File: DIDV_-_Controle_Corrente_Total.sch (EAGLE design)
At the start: 135 parts, among them IC401 PIC18F4550_TQFP44, K401 G5L, Q402 BC817, Q501 FZT493, Q502 FZT493, U201 ACS712LC, U202 ACS712LC, U203 ACS712LC, U301 LM35CAZ, U302 LM35CAZ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

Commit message: Revisão 7:
-  Alterações necessárias para adequação às necessidades dos exemplos de controle que temos.
-  Revisão da forma de filtragem de sinais digitais
-  Algumas nomenclaturas ainda estão erradas, deverão ser corrigidas com o andamento da implementação.
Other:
- note added: "07"
- note removed: "01"
- note removed: "06"
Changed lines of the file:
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@@
 <setting verticaltext="up"/>
 </settings>
-<grid distance="0.1" unitdist="inch" unit="inch" style="lines" multiple="1" display="yes" altdistance="0.01" altunitdist="inch" altunit="inch"/>
+<grid distance="0.1" unitdist="inch" unit="inch" style="lines" multiple="1" display="no" altdistance="0.01" altunitdist="inch" altunit="inch"/>
 <layers>
 <layer number="1" name="Top" color="4" fill="1" visible="no" active="no"/>
@@
 <text x="203.2" y="29.464" size="1.778" layer="150" font="vector">Dispositivo de Interface para</text>
 <text x="210.82" y="26.162" size="1.778" layer="150" font="vector">Deficientes Visuais</text>
-<text x="250.698" y="10.16" size="2.54" layer="150" font="vector">01</text>
+<text x="250.698" y="10.16" size="2.54" layer="150" font="vector">07</text>
 <text x="10.16" y="111.76" size="2.54" layer="97" font="vector">Conexao_Fonte_5V</text>
 <wire x1="7.62" y1="172.72" x2="7.62" y2="109.22" width="0.1524" layer="97" style="longdash"/>
@@
 <text x="203.2" y="29.464" size="1.778" layer="150" font="vector">Dispositivo de Interface para</text>
 <text x="210.82" y="26.162" size="1.778" layer="150" font="vector">Deficientes Visuais</text>
-<text x="250.698" y="10.16" size="2.54" layer="150" font="vector">01</text>
+<text x="250.698" y="10.16" size="2.54" layer="150" font="vector">07</text>
 <wire x1="10.16" y1="172.72" x2="10.16" y2="119.38" width="0.1524" layer="97" style="longdash"/>
 <wire x1="10.16" y1="119.38" x2="83.82" y2="119.38" width="0.1524" layer="97" style="longdash"/>
@@
 <text x="203.2" y="29.464" size="1.778" layer="150" font="vector">Dispositivo de Interface para</text>
 <text x="210.82" y="26.162" size="1.778" layer="150" font="vector">Deficientes Visuais</text>
-<text x="250.698" y="10.16" size="2.54" layer="150" font="vector">01</text>
+<text x="250.698" y="10.16" size="2.54" layer="150" font="vector">07</text>
 <wire x1="10.16" y1="172.72" x2="10.16" y2="119.38" width="0.1524" layer="97" style="longdash"/>
 <wire x1="10.16" y1="119.38" x2="83.82" y2="119.38" width="0.1524" layer="97" style="longdash"/>
@@
 <text x="203.2" y="29.464" size="1.778" layer="150" font="vector">Dispositivo de Interface para</text>
 <text x="210.82" y="26.162" size="1.778" layer="150" font="vector">Deficientes Visuais</text>
-<text x="250.698" y="10.16" size="2.54" layer="150" font="vector">06</text>
+<text x="250.698" y="10.16" size="2.54" layer="150" font="vector">07</text>
 <wire x1="5.08" y1="73.66" x2="5.08" y2="5.08" width="0.1524" layer="97" style="longdash"/>
 <wire x1="5.08" y1="5.08" x2="60.96" y2="5.08" width="0.1524" layer="97" style="longdash"/>
@@
 <text x="203.2" y="29.464" size="1.778" layer="150" font="vector">Dispositivo de Interface para</text>
 <text x="210.82" y="26.162" size="1.778" layer="150" font="vector">Deficientes Visuais</text>
-<text x="250.698" y="10.16" size="2.54" layer="150" font="vector">06</text>
+<text x="250.698" y="10.16" size="2.54" layer="150" font="vector">07</text>
 <text x="12.7" y="91.44" size="2.54" layer="97" font="vector">Cooler1</text>
 <wire x1="10.16" y1="88.9" x2="104.14" y2="88.9" width="0.1524" layer="97" style="longdash"/>

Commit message: Revisão 8:
-  Add Circuito Buck
-  Alterações funcionais
-   Inserção dos primeiros boards
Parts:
- removed D401, D402: (no value), led:LEDMINI-TOP
- removed R403, R404: 270, rcl:R-US_R0603
- removed R406, R407: 22R, rcl:R-US_R0603
- removed X401: MINI-USB-32005-301, con-cypressindustries:MINI-USB-32005-301
- added C601, C602: 10n, rcl:C-USC0603K
- added D102, D103: ESDAXXL, diode:ESDAXXL
- added D601, D602: (no value), led:LEDMINI-TOP
- added Q602, Q604: (no value), transistor:BC817-25LT1-NPN-SOT23-BEC
- added R1, R2: 22R, rcl:R-US_R0603
- added R601, R606: 10k, rcl:R-US_R0603
- added R602, R605: 100k, rcl:R-US_R0603
- added R603, R604: 270, rcl:R-US_R0603
- added X101: MINI-USB-32005-301, con-cypressindustries:MINI-USB-32005-301
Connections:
- net -3V3 renamed _VCC
- net AN_3V3 renamed AN_6V
- net N$27 renamed 12V_EN
- net _+3V3 renamed _6V
- removed net +3V3: C103.+, JP118.1, JP120.1, JP127.2, R103.2, U202.IP+, U202.IP+@2
- removed net AN_3V3_: C210.1, R202.1, R205.1
- removed net C1: IC401.RC2/CCP1/P1A, R503.1
- removed net C2: IC401.RB3/AN9/CCP2/VPO, R501.1
- removed net N$16: IC401.RA5/AN4/!SS!/HLVDIN/C2OUT
- removed net N$24: IC401.RA2/AN2/VREF-/CVREF
- removed net N$32: IC401.RA3/AN3/VREF+
- removed net N$34: IC401.RA0/AN0
- new net +6V: C103.+, JP118.1, JP120.1, JP127.2, R103.2
- new net 6V: U202.IP+, U202.IP+@2
- new net AN_6V_: C210.1, IC401.RA2/AN2/VREF-/CVREF, R202.1, R205.1
- new net COOLERS: IC401.RC2/CCP1/P1A, R501.1, R503.1
- new net CTRL_B: IC401.RB3/AN9/CCP2/VPO
- new net N$33: D103.C1, R2.1, X101.2
- new net N$37: D102.C1, R1.1, X101.3
- net +D: now also R1.2; no longer R406.2
- net -D: now also R2.2; no longer R407.2
- net AN_12V_: now also IC401.RA3/AN3/VREF+
- net AN_VCC_: now also IC401.RA0/AN0
- net GND: now also C601.2, C602.2, D102.C2, D103.C2, Q602.E, Q604.E, R602.2, R605.2, X101.5; no longer D401.C, D402.C, X401.5
- net N$10: now also D602.A, R604.2; no longer R406.1, X401.3
- net N$13: now also C601.1, Q604.B, R601.1, R602.1; no longer IC401.RE2/AN7/OESPP
- net N$15: now also C602.1, Q602.B, R605.1, R606.2; no longer IC401.RE0/AN5/CK1SPP
- net N$30: now also D601.C, Q604.C; no longer D402.A, R403.1
- net N$31: now also D602.C, Q602.C; no longer D401.A, R404.2
- net N$9: now also D601.A, R603.1; no longer R407.1, X401.2
- net TS1_: now also IC401.RA5/AN4/!SS!/HLVDIN/C2OUT
- net TS2_: now also IC401.RE0/AN5/CK1SPP
- net TS3_: now also IC401.RE2/AN7/OESPP
- net USBCON: now also R601.2; no longer R403.2
- net USBTXRX: now also R606.1; no longer R404.1
- net VCC: now also R603.2, R604.1
- net VUSB: now also X101.1; no longer X401.1
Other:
- note added: "08"
- note added: "Conexao_Fonte_6V"
- note added: "Leds Indicadores"
- note removed: "07"
- note removed: "Conexao_Fonte_3V3"
- moved on the sheet: C404, C405, C408, C501, C502, D403, R405, R411, R413, S401

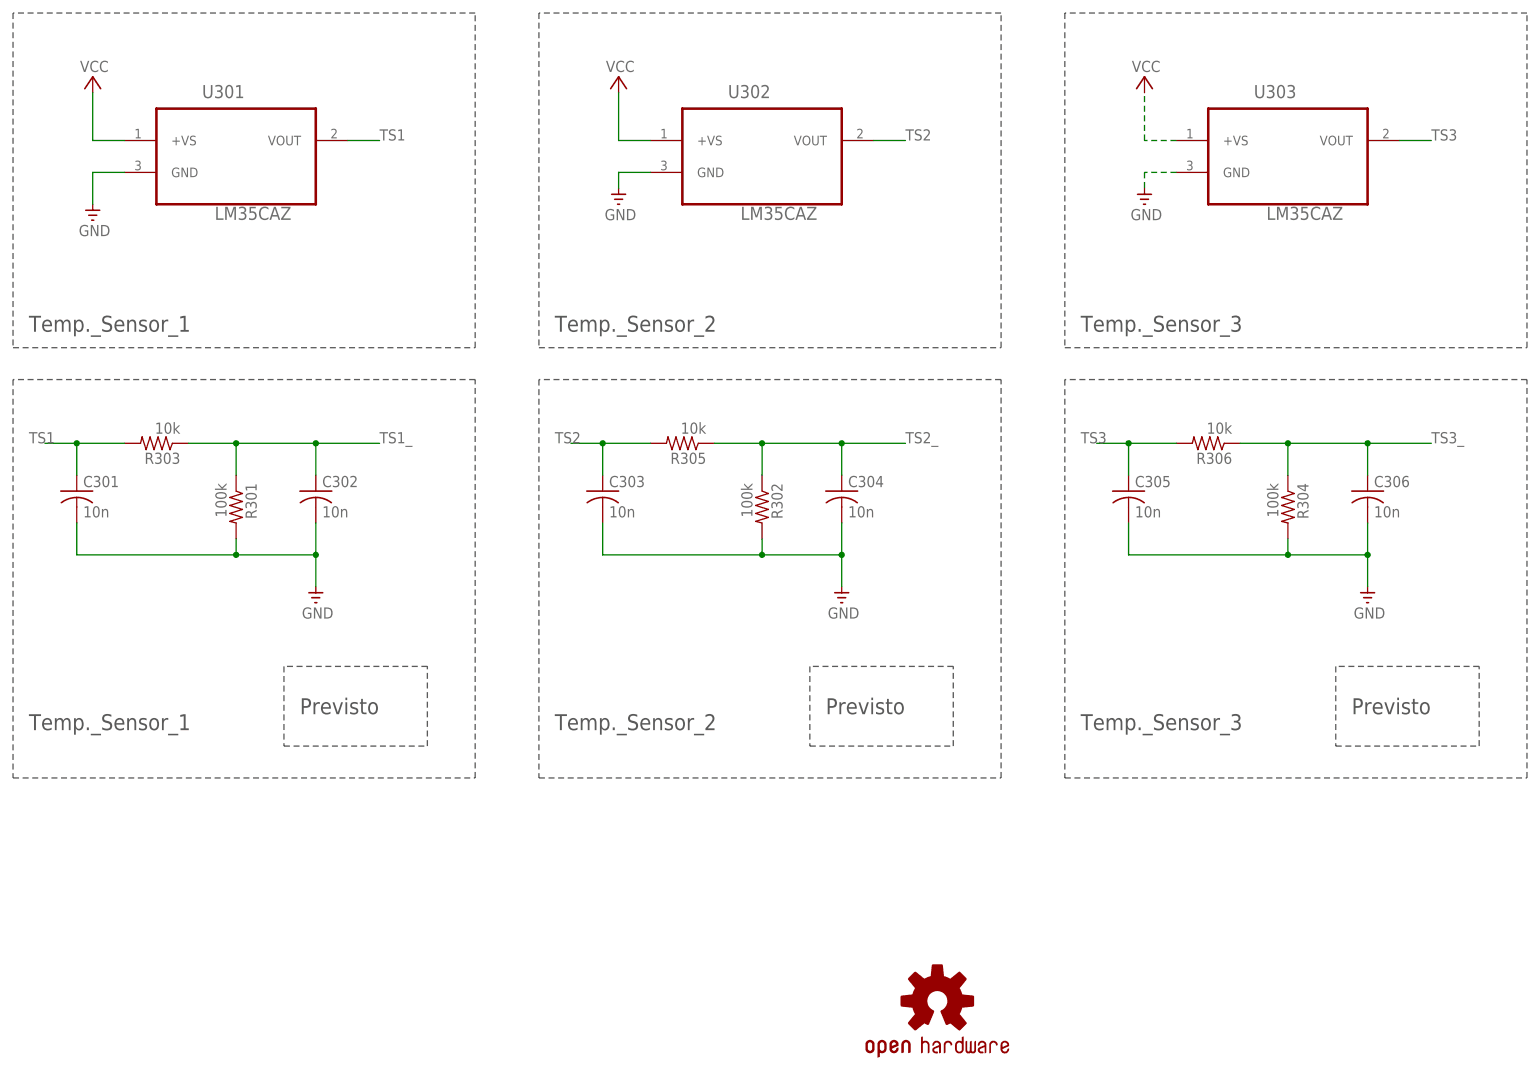
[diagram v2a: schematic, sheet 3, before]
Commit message: Revisão 9
- Corrigidos algumas falhas de ligação
- Implementação com VPRG dos TLCs via Hardware
- Inserção do cálculo do Riref

Obs. Se somente a criação de boards, não será incrementado. No caso, se criado um board novo board vou subir para 9.1 e assim por diante.
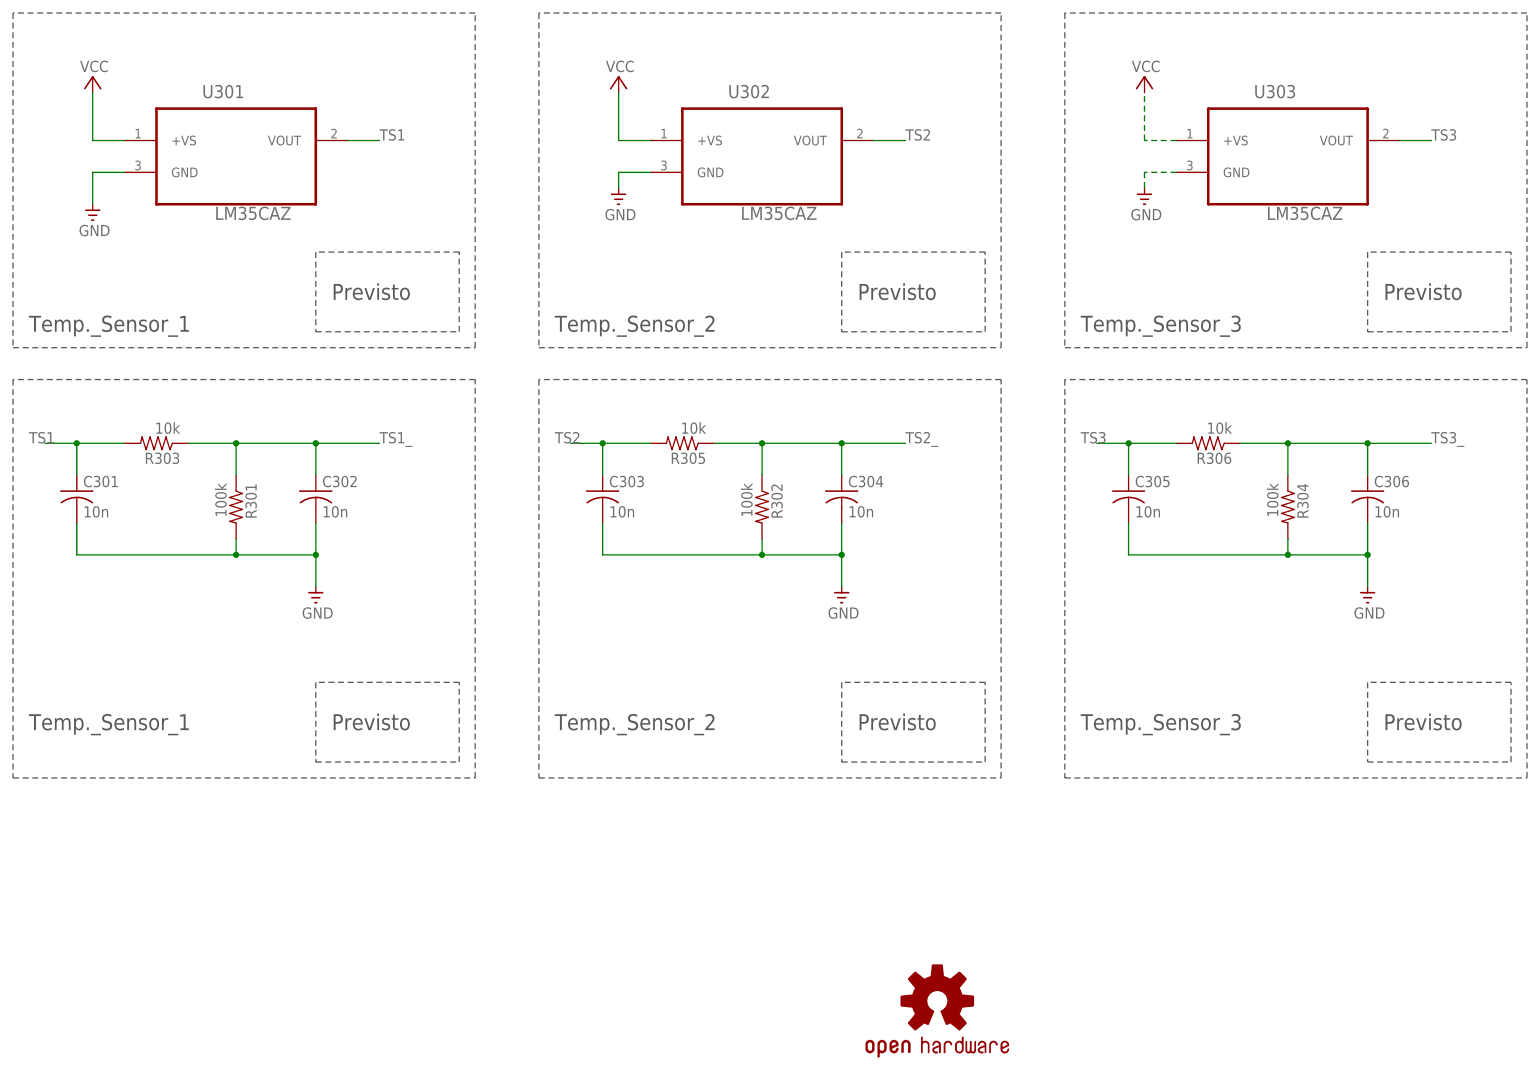
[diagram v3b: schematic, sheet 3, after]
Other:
- note added: "09"
- note removed: "08"
